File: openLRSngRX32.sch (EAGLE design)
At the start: 58 parts, among them IC1 STM32F10XCXT6, IC2 REG1117, U1 MPU-6000QFN-24, Y1 8MHz

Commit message: cleanup
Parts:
- LED1: value (none) -> RED
- LED2: value (none) -> GREEN
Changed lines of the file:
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@@
 <part name="JP11" library="SparkFun-Connectors" deviceset="M02" device="PTH"/>
 <part name="C17" library="SparkFun-Capacitors" deviceset="CAP" device="0805"/>
-<part name="LED1" library="led" deviceset="LED" device="SML0805"/>
-<part name="LED2" library="led" deviceset="LED" device="SML0805"/>
+<part name="LED1" library="led" deviceset="LED" device="SML0805" value="RED"/>
+<part name="LED2" library="led" deviceset="LED" device="SML0805" value="GREEN"/>
 <part name="R18" library="SparkFun-Resistors" deviceset="RESISTOR" device="0805-RES" value="330R"/>
 <part name="R19" library="SparkFun-Resistors" deviceset="RESISTOR" device="0805-RES" value="330R"/>

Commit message: GB leds
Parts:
- added LED3: RED, led:LEDSML0805
- added R20: 330R, SparkFun-Resistors:RESISTOR0805-RES
- LED1: value RED -> GRN
- LED2: value GREEN -> BLU
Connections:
- removed net N$29: LED1.C, R18.2
- new net N$33: IC1PORTA_H.PA11, R20.2
- new net N$34: IC1PORTA_H.PA12, R18.2
- new net N$35: IC1PORTA_H.PA13, R19.2
- net GND: now also LED1.C, LED2.C, LED3.C; no longer R18.1, R19.1
- net N$30: now also LED3.A, R20.1; no longer LED2.C, R19.2
- net N$31: now also R18.1; no longer IC1PORTA_H.PA11
- net N$32: now also R19.1; no longer IC1PORTA_H.PA14
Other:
- moved on the sheet: LED1, LED2, R18, R19
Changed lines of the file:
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@@
 <part name="JP11" library="SparkFun-Connectors" deviceset="M02" device="PTH"/>
 <part name="C17" library="SparkFun-Capacitors" deviceset="CAP" device="0805"/>
-<part name="LED1" library="led" deviceset="LED" device="SML0805" value="RED"/>
-<part name="LED2" library="led" deviceset="LED" device="SML0805" value="GREEN"/>
+<part name="LED1" library="led" deviceset="LED" device="SML0805" value="GRN"/>
+<part name="LED2" library="led" deviceset="LED" device="SML0805" value="BLU"/>
 <part name="R18" library="SparkFun-Resistors" deviceset="RESISTOR" device="0805-RES" value="330R"/>
 <part name="R19" library="SparkFun-Resistors" deviceset="RESISTOR" device="0805-RES" value="330R"/>
 <part name="GND18" library="supply1" deviceset="GND" device=""/>
+<part name="LED3" library="led" deviceset="LED" device="SML0805" value="RED"/>
+<part name="R20" library="SparkFun-Resistors" deviceset="RESISTOR" device="0805-RES" value="330R"/>
 </parts>
 <sheets>
@@
 <instance part="JP11" gate="G$1" x="-45.72" y="22.86"/>
 <instance part="C17" gate="G$1" x="-78.74" y="33.02"/>
-<instance part="LED1" gate="G$1" x="27.94" y="58.42" rot="R270"/>
-<instance part="LED2" gate="G$1" x="27.94" y="53.34" rot="R270"/>
-<instance part="R18" gate="G$1" x="15.24" y="58.42"/>
-<instance part="R19" gate="G$1" x="15.24" y="53.34"/>
+<instance part="LED1" gate="G$1" x="22.86" y="55.88" rot="R270"/>
+<instance part="LED2" gate="G$1" x="22.86" y="50.8" rot="R270"/>
+<instance part="R18" gate="G$1" x="33.02" y="55.88"/>
+<instance part="R19" gate="G$1" x="33.02" y="50.8"/>
 <instance part="GND18" gate="1" x="5.08" y="48.26"/>
+<instance part="LED3" gate="G$1" x="22.86" y="60.96" rot="R270"/>
+<instance part="R20" gate="G$1" x="33.02" y="60.96"/>
 </instances>
 <busses>
@@
 </segment>
 <segment>
+<pinref part="LED3" gate="G$1" pin="C"/>
+<pinref part="LED1" gate="G$1" pin="C"/>
+<wire x1="17.78" y1="60.96" x2="17.78" y2="55.88" width="0.1524" layer="91"/>
+<pinref part="LED2" gate="G$1" pin="C"/>
+<wire x1="17.78" y1="55.88" x2="17.78" y2="50.8" width="0.1524" layer="91"/>
 <pinref part="GND18" gate="1" pin="GND"/>
-<pinref part="R19" gate="G$1" pin="1"/>
-<wire x1="5.08" y1="50.8" x2="5.08" y2="53.34" width="0.1524" layer="91"/>
-<wire x1="5.08" y1="53.34" x2="10.16" y2="53.34" width="0.1524" layer="91"/>
-<pinref part="R18" gate="G$1" pin="1"/>
-<wire x1="5.08" y1="53.34" x2="5.08" y2="58.42" width="0.1524" layer="91"/>
-<wire x1="5.08" y1="58.42" x2="10.16" y2="58.42" width="0.1524" layer="91"/>
-<junction x="5.08" y="53.34"/>
+<wire x1="17.78" y1="50.8" x2="5.08" y2="50.8" width="0.1524" layer="91"/>
+<junction x="17.78" y="55.88"/>
+<junction x="17.78" y="50.8"/>
 </segment>
 </net>
@@
 </segment>
 </net>
-<net name="N$29" class="0">
-<segment>
-<pinref part="R18" gate="G$1" pin="2"/>
-<pinref part="LED1" gate="G$1" pin="C"/>
-<wire x1="20.32" y1="58.42" x2="22.86" y2="58.42" width="0.1524" layer="91"/>
-</segment>
-</net>
 <net name="N$30" class="0">
 <segment>
-<pinref part="R19" gate="G$1" pin="2"/>
-<pinref part="LED2" gate="G$1" pin="C"/>
-<wire x1="20.32" y1="53.34" x2="22.86" y2="53.34" width="0.1524" layer="91"/>
+<pinref part="LED3" gate="G$1" pin="A"/>
+<pinref part="R20" gate="G$1" pin="1"/>
+<wire x1="25.4" y1="60.96" x2="27.94" y2="60.96" width="0.1524" layer="91"/>
 </segment>
 </net>
@@
 <segment>
 <pinref part="LED1" gate="G$1" pin="A"/>
-<wire x1="30.48" y1="58.42" x2="35.56" y2="58.42" width="0.1524" layer="91"/>
-<wire x1="35.56" y1="58.42" x2="38.1" y2="60.96" width="0.1524" layer="91"/>
+<pinref part="R18" gate="G$1" pin="1"/>
+<wire x1="25.4" y1="55.88" x2="27.94" y2="55.88" width="0.1524" layer="91"/>
+</segment>
+</net>
+<net name="N$32" class="0">
+<segment>
+<pinref part="LED2" gate="G$1" pin="A"/>
+<pinref part="R19" gate="G$1" pin="1"/>
+<wire x1="25.4" y1="50.8" x2="27.94" y2="50.8" width="0.1524" layer="91"/>
+</segment>
+</net>
+<net name="N$33" class="0">
+<segment>
+<pinref part="R20" gate="G$1" pin="2"/>
 <pinref part="IC1" gate="PORTA_H" pin="PA11"/>
 <wire x1="38.1" y1="60.96" x2="48.26" y2="60.96" width="0.1524" layer="91"/>
 </segment>
 </net>
-<net name="N$32" class="0">
-<segment>
-<pinref part="LED2" gate="G$1" pin="A"/>
-<pinref part="IC1" gate="PORTA_H" pin="PA14"/>
-<wire x1="30.48" y1="53.34" x2="48.26" y2="53.34" width="0.1524" layer="91"/>
-</segment>
-</net>
+<net name="N$34" class="0">
+<segment>
+<pinref part="R18" gate="G$1" pin="2"/>
+<wire x1="38.1" y1="55.88" x2="40.64" y2="55.88" width="0.1524" layer="91"/>
+<wire x1="40.64" y1="55.88" x2="40.64" y2="58.42" width="0.1524" layer="91"/>
+<pinref part="IC1" gate="PORTA_H" pin="PA12"/>
+<wire x1="40.64" y1="58.42" x2="48.26" y2="58.42" width="0.1524" layer="91"/>
+</segment>
+</net>
+<net name="N$35" class="0">
+<segment>
+<pinref part="R19" gate="G$1" pin="2"/>
+<wire x1="38.1" y1="50.8" x2="43.18" y2="50.8" width="0.1524" layer="91"/>
+<wire x1="43.18" y1="50.8" x2="43.18" y2="55.88" width="0.1524" layer="91"/>
+<pinref part="IC1" gate="PORTA_H" pin="PA13"/>
+<wire x1="43.18" y1="55.88" x2="48.26" y2="55.88" width="0.1524" layer="91"/>
+</segment>
+</net>

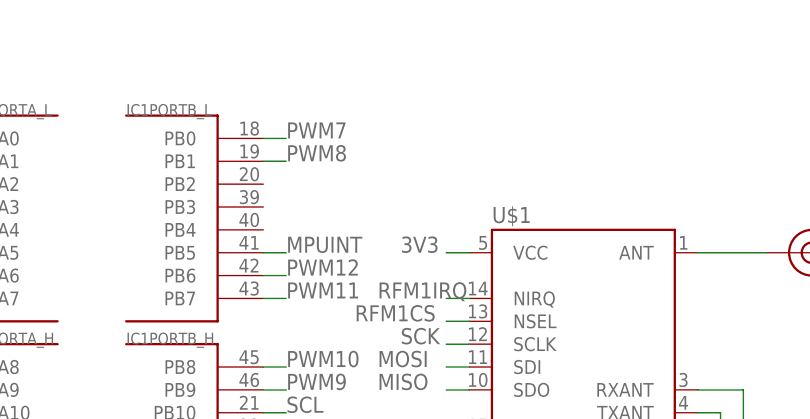
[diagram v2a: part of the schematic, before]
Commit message: Fix missing BOOT1 pulldown.
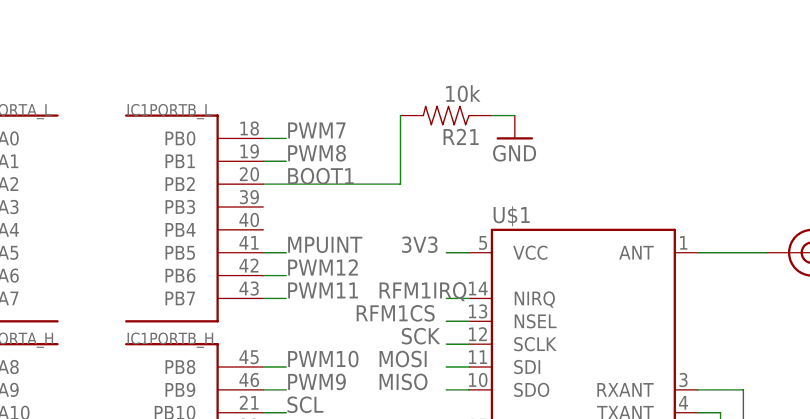
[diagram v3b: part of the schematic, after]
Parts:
- added R21: 10k, SparkFun-Resistors:RESISTOR0805-RES
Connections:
- new net BOOT1: IC1PORTB_L.PB2, R21.2
- net GND: now also R21.1
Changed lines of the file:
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@@
 <part name="LED3" library="led" deviceset="LED" device="SML0805" value="RED"/>
 <part name="R20" library="SparkFun-Resistors" deviceset="RESISTOR" device="0805-RES" value="330R"/>
+<part name="R21" library="SparkFun-Resistors" deviceset="RESISTOR" device="0805-RES" value="10k"/>
+<part name="GND19" library="supply1" deviceset="GND" device=""/>
 </parts>
 <sheets>
@@
 <instance part="LED3" gate="G$1" x="22.86" y="60.96" rot="R270"/>
 <instance part="R20" gate="G$1" x="33.02" y="60.96"/>
+<instance part="R21" gate="G$1" x="106.68" y="96.52" rot="R180"/>
+<instance part="GND19" gate="1" x="114.3" y="93.98"/>
 </instances>
 <busses>
@@
 <junction x="17.78" y="50.8"/>
 </segment>
+<segment>
+<pinref part="R21" gate="G$1" pin="1"/>
+<pinref part="GND19" gate="1" pin="GND"/>
+<wire x1="111.76" y1="96.52" x2="114.3" y2="96.52" width="0.1524" layer="91"/>
+</segment>
 </net>
 <net name="VCC" class="0">
@@
 </segment>
 </net>
+<net name="BOOT1" class="0">
+<segment>
+<pinref part="IC1" gate="PORTB_L" pin="PB2"/>
+<pinref part="R21" gate="G$1" pin="2"/>
+<wire x1="86.36" y1="88.9" x2="101.6" y2="88.9" width="0.1524" layer="91"/>
+<wire x1="101.6" y1="88.9" x2="101.6" y2="96.52" width="0.1524" layer="91"/>
+<label x="88.9" y="88.9" size="1.778" layer="95"/>
+</segment>
+</net>
